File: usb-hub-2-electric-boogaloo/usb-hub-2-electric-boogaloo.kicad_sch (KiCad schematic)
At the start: 39 parts, among them U1 SL2.1S, U2 GL823K-HCY04

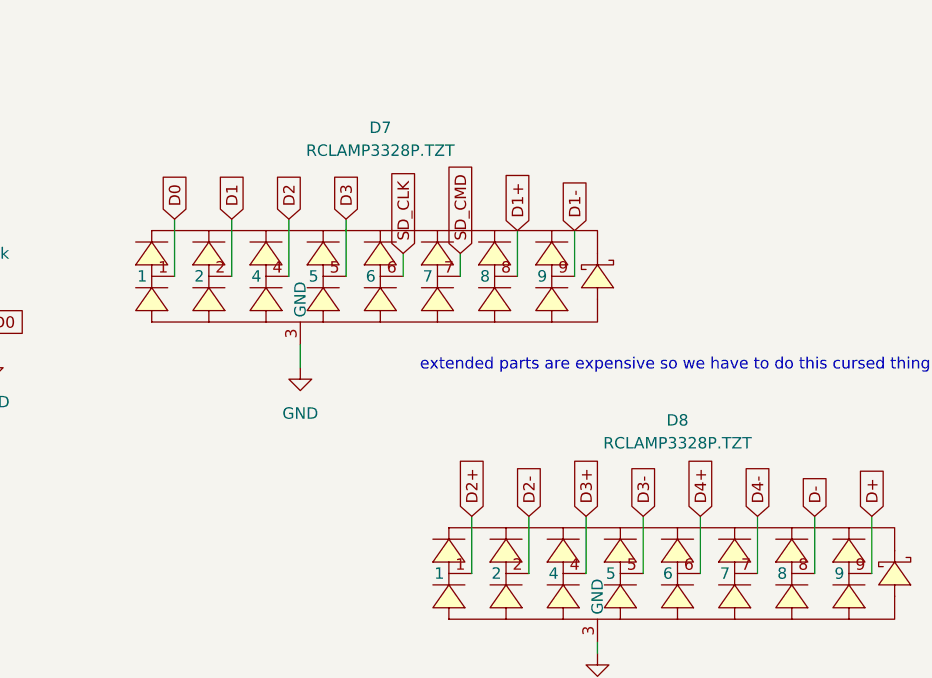
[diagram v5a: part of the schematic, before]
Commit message: finish main routing (still disconnects tho)
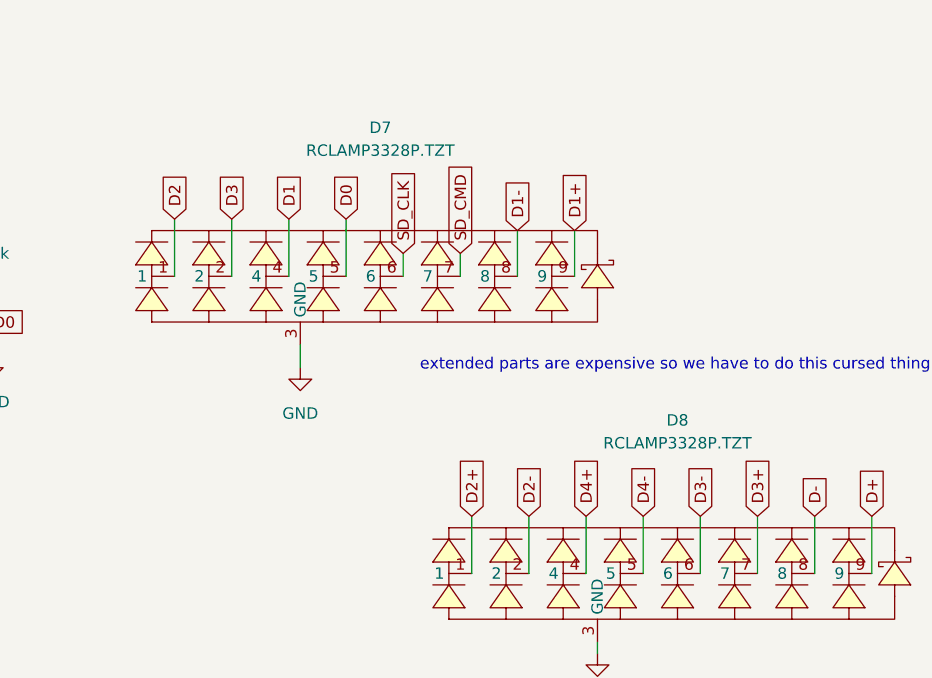
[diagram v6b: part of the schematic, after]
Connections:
- net D0: now also D7.5; no longer D7.1
- net D1: now also D7.4; no longer D7.2
- net D1+: now also D7.9; no longer D7.8
- net D1-: now also D7.8; no longer D7.9
- net D2: now also D7.1; no longer D7.4
- net D3: now also D7.2; no longer D7.5
- net D3+: now also D8.7; no longer D8.4
- net D3-: now also D8.6; no longer D8.5
- net D4+: now also D8.4; no longer D8.6
- net D4-: now also D8.5; no longer D8.7

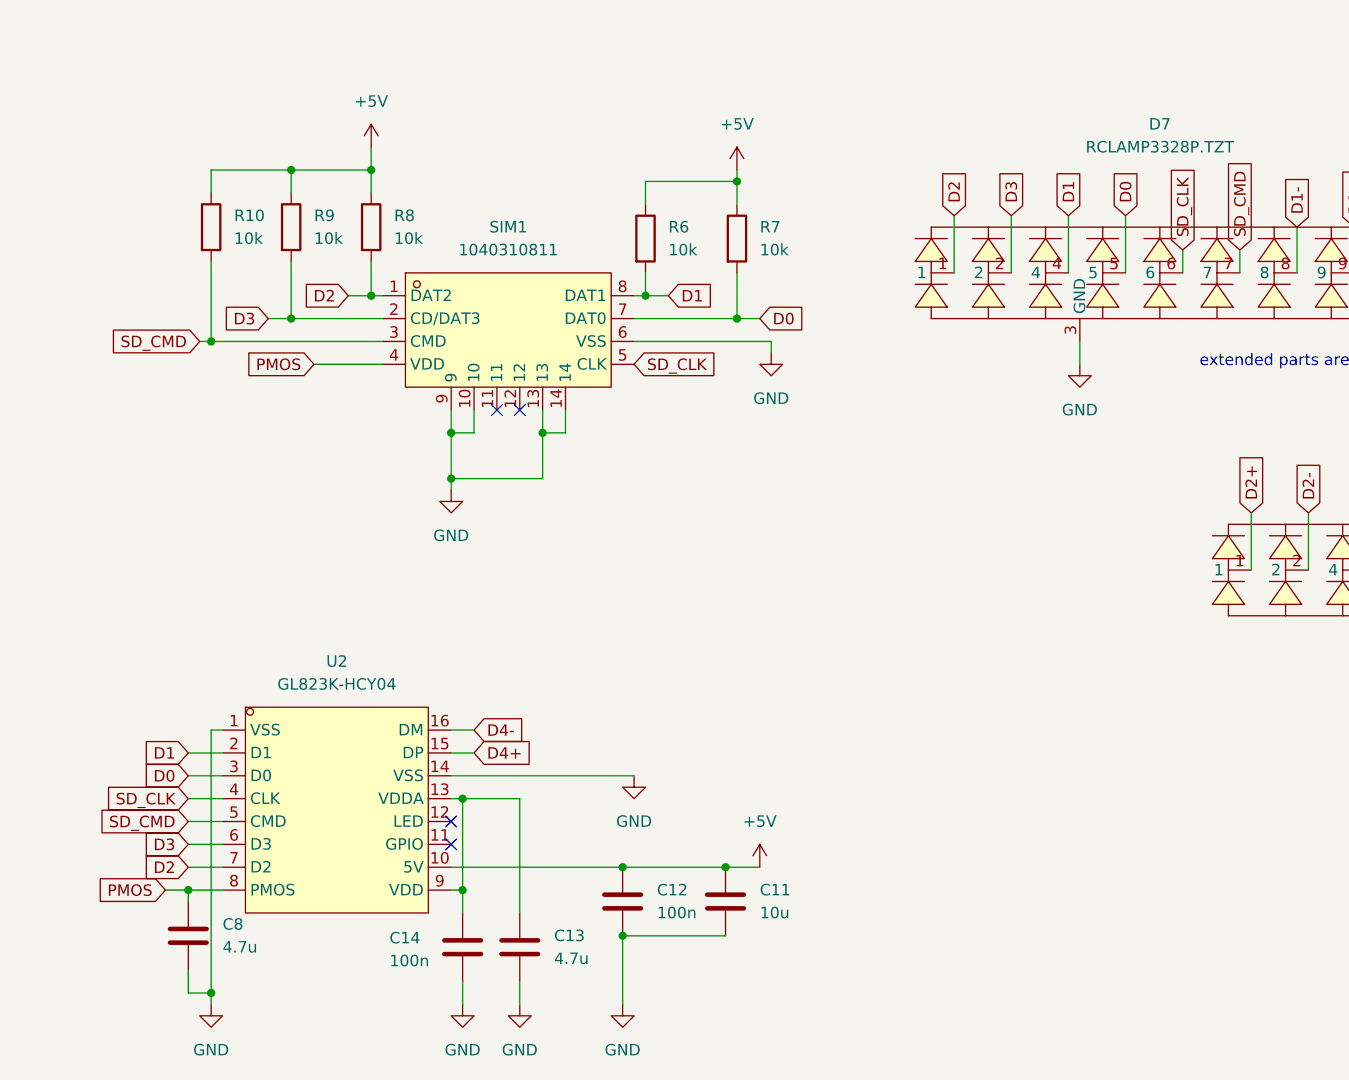
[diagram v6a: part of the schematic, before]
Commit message: vias and mounting holes
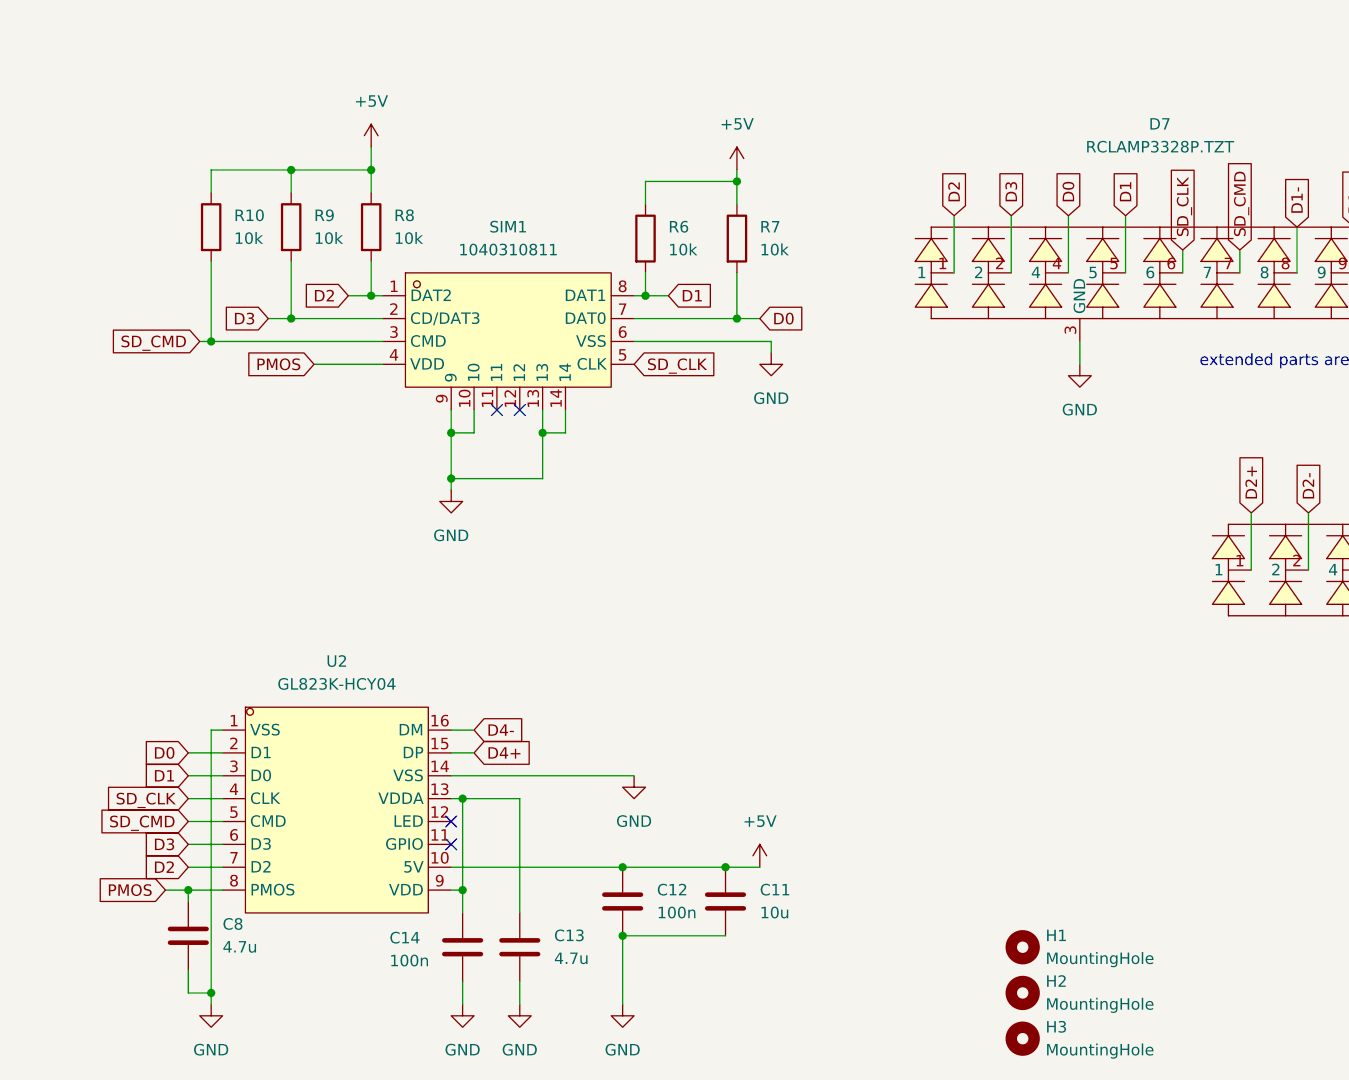
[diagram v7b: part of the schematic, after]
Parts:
- added H1, H2, H3: MountingHole, MountingHole:MountingHole_2.2mm_M2, symbol Mechanical:MountingHole
- R6, R7: footprint Resistor_SMD:R_0603_1608Metric_Pad0.98x0.95mm_HandSolder -> Resistor_SMD:R_0402_1005Metric_Pad0.72x0.64mm_HandSolder
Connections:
- net D0: now also D7.4, U2.2 (D1); no longer D7.5, U2.3 (D0)
- net D1: now also D7.5, U2.3 (D0); no longer D7.4, U2.2 (D1)
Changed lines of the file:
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@@
 	(global_label "D0"
 		(shape input)
-		(at 134.62 92.71 90)
+		(at 128.27 92.71 90)
 		(fields_autoplaced yes)
 		(effects
@@
 		)
 		(property "Intersheetrefs" "${INTERSHEET_REFS}"
-			(at 134.62 87.2453 90)
+			(at 128.27 87.2453 90)
 			(hide yes)
 			(show_name no)
@@
 	(global_label "D1"
 		(shape input)
-		(at 128.27 92.71 90)
+		(at 134.62 92.71 90)
 		(fields_autoplaced yes)
 		(effects
@@
 		)
 		(property "Intersheetrefs" "${INTERSHEET_REFS}"
-			(at 128.27 87.2453 90)
+			(at 134.62 87.2453 90)
 			(hide yes)
 			(show_name no)
@@
 	(global_label "D1"
 		(shape input)
-		(at 30.48 152.4 180)
+		(at 30.48 154.94 180)
 		(fields_autoplaced yes)
 		(effects
@@
 		)
 		(property "Intersheetrefs" "${INTERSHEET_REFS}"
-			(at 25.0153 152.4 0)
+			(at 25.0153 154.94 0)
 			(hide yes)
 			(show_name no)
@@
 	(global_label "D0"
 		(shape input)
-		(at 30.48 154.94 180)
+		(at 30.48 152.4 180)
 		(fields_autoplaced yes)
 		(effects
@@
 		)
 		(property "Intersheetrefs" "${INTERSHEET_REFS}"
-			(at 25.0153 154.94 0)
+			(at 25.0153 152.4 0)
 			(hide yes)
 			(show_name no)
@@
 	)
 	(symbol
+		(lib_id "Mechanical:MountingHole")
+		(at 123.19 184.15 0)
+		(unit 1)
+		(body_style 1)
+		(exclude_from_sim no)
+		(in_bom no)
+		(on_board yes)
+		(in_pos_files yes)
+		(dnp no)
+		(fields_autoplaced yes)
+		(property "Reference" "H3"
+			(at 125.73 182.8799 0)
+			(show_name no)
+			(do_not_autoplace no)
+			(effects
+				(font
+					(size 1.27 1.27)
+				)
+				(justify left)
+			)
+		)
+		(property "Value" "MountingHole"
+			(at 125.73 185.4199 0)
+			(show_name no)
+			(do_not_autoplace no)
+			(effects
+				(font
+					(size 1.27 1.27)
+				)
+				(justify left)
+			)
+		)
+		(property "Footprint" "MountingHole:MountingHole_2.2mm_M2"
+			(at 123.19 184.15 0)
+			(hide yes)
+			(show_name no)
+			(do_not_autoplace no)
+			(effects
+				(font
+					(size 1.27 1.27)
+				)
+			)
+		)
+		(property "Datasheet" ""
+			(at 123.19 184.15 0)
+			(hide yes)
+			(show_name no)
+			(do_not_autoplace no)
+			(effects
+				(font
+					(size 1.27 1.27)
+				)
+			)
+		)
+		(property "Description" "Mounting Hole without connection"
+			(at 123.19 184.15 0)
+			(hide yes)
+			(show_name no)
+			(do_not_autoplace no)
+			(effects
+				(font
+					(size 1.27 1.27)
+				)
+			)
+		)
+		(instances
+			(project "usb-hub-2-electric-boogaloo"
+				(path "/258ca4ed-9343-4248-9111-37b15314376b"
+					(reference "H3")
+					(unit 1)
+				)
+			)
+		)
+	)
+	(symbol
 		(lib_id "Device:C")
 		(at 149.86 52.07 0)
@@
 	)
 	(symbol
+		(lib_id "Mechanical:MountingHole")
+		(at 123.19 173.99 0)
+		(unit 1)
+		(body_style 1)
+		(exclude_from_sim no)
+		(in_bom no)
+		(on_board yes)
+		(in_pos_files yes)
+		(dnp no)
+		(fields_autoplaced yes)
+		(property "Reference" "H1"
+			(at 125.73 172.7199 0)
+			(show_name no)
+			(do_not_autoplace no)
+			(effects
+				(font
+					(size 1.27 1.27)
+				)
+				(justify left)
+			)
+		)
+		(property "Value" "MountingHole"
+			(at 125.73 175.2599 0)
+			(show_name no)
+			(do_not_autoplace no)
+			(effects
+				(font
+					(size 1.27 1.27)
+				)
+				(justify left)
+			)
+		)
+		(property "Footprint" "MountingHole:MountingHole_2.2mm_M2"
+			(at 123.19 173.99 0)
+			(hide yes)
+			(show_name no)
+			(do_not_autoplace no)
+			(effects
+				(font
+					(size 1.27 1.27)
+				)
+			)
+		)
+		(property "Datasheet" ""
+			(at 123.19 173.99 0)
+			(hide yes)
+			(show_name no)
+			(do_not_autoplace no)
+			(effects
+				(font
+					(size 1.27 1.27)
+				)
+			)
+		)
+		(property "Description" "Mounting Hole without connection"
+			(at 123.19 173.99 0)
+			(hide yes)
+			(show_name no)
+			(do_not_autoplace no)
+			(effects
+				(font
+					(size 1.27 1.27)
+				)
+			)
+		)
+		(instances
+			(project "usb-hub-2-electric-boogaloo"
+				(path "/258ca4ed-9343-4248-9111-37b15314376b"
+					(reference "H1")
+					(unit 1)
+				)
+			)
+		)
+	)
+	(symbol
 		(lib_id "power:GND")
 		(at 167.64 35.56 0)
@@
 			)
 		)
-		(property "Footprint" "Resistor_SMD:R_0603_1608Metric_Pad0.98x0.95mm_HandSolder"
+		(property "Footprint" "Resistor_SMD:R_0402_1005Metric_Pad0.72x0.64mm_HandSolder"
 			(at 79.502 95.25 90)
 			(hide yes)
@@
 			)
 		)
-		(property "Footprint" "Resistor_SMD:R_0603_1608Metric_Pad0.98x0.95mm_HandSolder"
+		(property "Footprint" "Resistor_SMD:R_0402_1005Metric_Pad0.72x0.64mm_HandSolder"
 			(at 89.662 95.25 90)
 			(hide yes)
@@
 					(unit 1)
 				)
+			)
+		)
+	)
+	(symbol
+		(lib_id "Mechanical:MountingHole")
+		(at 123.19 179.07 0)
+		(unit 1)
+		(body_style 1)
+		(exclude_from_sim no)
+		(in_bom no)
+		(on_board yes)
+		(in_pos_files yes)
+		(dnp no)
+		(fields_autoplaced yes)
+		(property "Reference" "H2"
+			(at 125.73 177.7999 0)
+			(show_name no)
+			(do_not_autoplace no)
+			(effects
+				(font
+					(size 1.27 1.27)
+				)
+				(justify left)
+			)
+		)
+		(property "Value" "MountingHole"
+			(at 125.73 180.3399 0)
+			(show_name no)
+			(do_not_autoplace no)
+			(effects
+				(font
+					(size 1.27 1.27)
+				)
+				(justify left)
+			)
+		)
+		(property "Footprint" "MountingHole:MountingHole_2.2mm_M2"
+			(at 123.19 179.07 0)
+			(hide yes)
+			(show_name no)
+			(do_not_autoplace no)
+			(effects
+				(font
+					(size 1.27 1.27)
+				)
+			)
+		)
+		(property "Datasheet" ""
+			(at 123.19 179.07 0)
+			(hide yes)
+			(show_name no)
+			(do_not_autoplace no)
+			(effects
+				(font
+					(size 1.27 1.27)
+				)
+			)
+		)
+		(property "Description" "Mounting Hole without connection"
+			(at 123.19 179.07 0)
+			(hide yes)
+			(show_name no)
+			(do_not_autoplace no)
+			(effects
+				(font
+					(size 1.27 1.27)
+				)
+			)
+		)
+		(instances
+			(project "usb-hub-2-electric-boogaloo"
+				(path "/258ca4ed-9343-4248-9111-37b15314376b"
+					(reference "H2")
+					(unit 1)
+				)

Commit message: fix usb + new renders
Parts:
- removed USB5: GT-USB-8016B, easyeda2kicad:USB-SMD_GT-USB-8016B, symbol easyeda2kicad:GT-USB-8016B
- added USB1: TYPE-C 16PIN 2MD, easyeda2kicad:USB-C-SMD_TYPE-C-16PIN-2MD-073, symbol easyeda2kicad:TYPE-C16PIN2MD
- R4: renamed from R1; footprint Resistor_SMD:R_0603_1608Metric_Pad0.98x0.95mm_HandSolder -> Resistor_SMD:R_0402_1005Metric_Pad0.72x0.64mm_HandSolder
- renumbered C8 to C1, C9 to C10, C7 to C11, C6 to C12, C3 to C13, C17 to C14, C18 to C15, C16 to C2, C14 to C3, C13 to C4, C12 to C5, C11 to C6, C15 to C7, C4 to C8, C10 to C9, D2 to D1, D7 to D2, D8 to D3, D1 to D4, D3 to D5, D4 to D6, D5 to D7, R10 to R1, R2 to R10, R9 to R2, R8 to R3, R6 to R5, R7 to R6, R4 to R7, R5 to R8, R3 to R9, U2 to U1, U1 to U2, USB3 to USB2, USB1 to USB3, USB2 to USB4
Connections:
- net D+: now also USB1.A6 (Dp1), USB1.B6 (Dp2)
- net D-: now also USB1.A7 (Dn1), USB1.B7 (Dn2)
- net GND: now also USB1.13 (EH), USB1.14 (EH), USB1.A1B12 (GND), USB1.B1A12 (GND)
- net at R4.1: now also USB1.A5 (CC1)
- net VBUS_D: now reaches C2.1, D1.1 (K)
- net VBUS_D: now also USB1.A4B9 (VBUS), USB1.B4A9 (VBUS)
- no-connect marks 14 -> 12
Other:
- moved on the sheet: C2, D1, R4
